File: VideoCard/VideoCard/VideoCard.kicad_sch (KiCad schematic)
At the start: 16 parts, among them J17 Conn_Coaxial, Q3 NPN, U12 TMS9918A, U16 74LS574, U17 74LS574, U18 74LS574, U19 HM62256BLP, U20 74HC04, U21 74LS138, Y1 Crystal

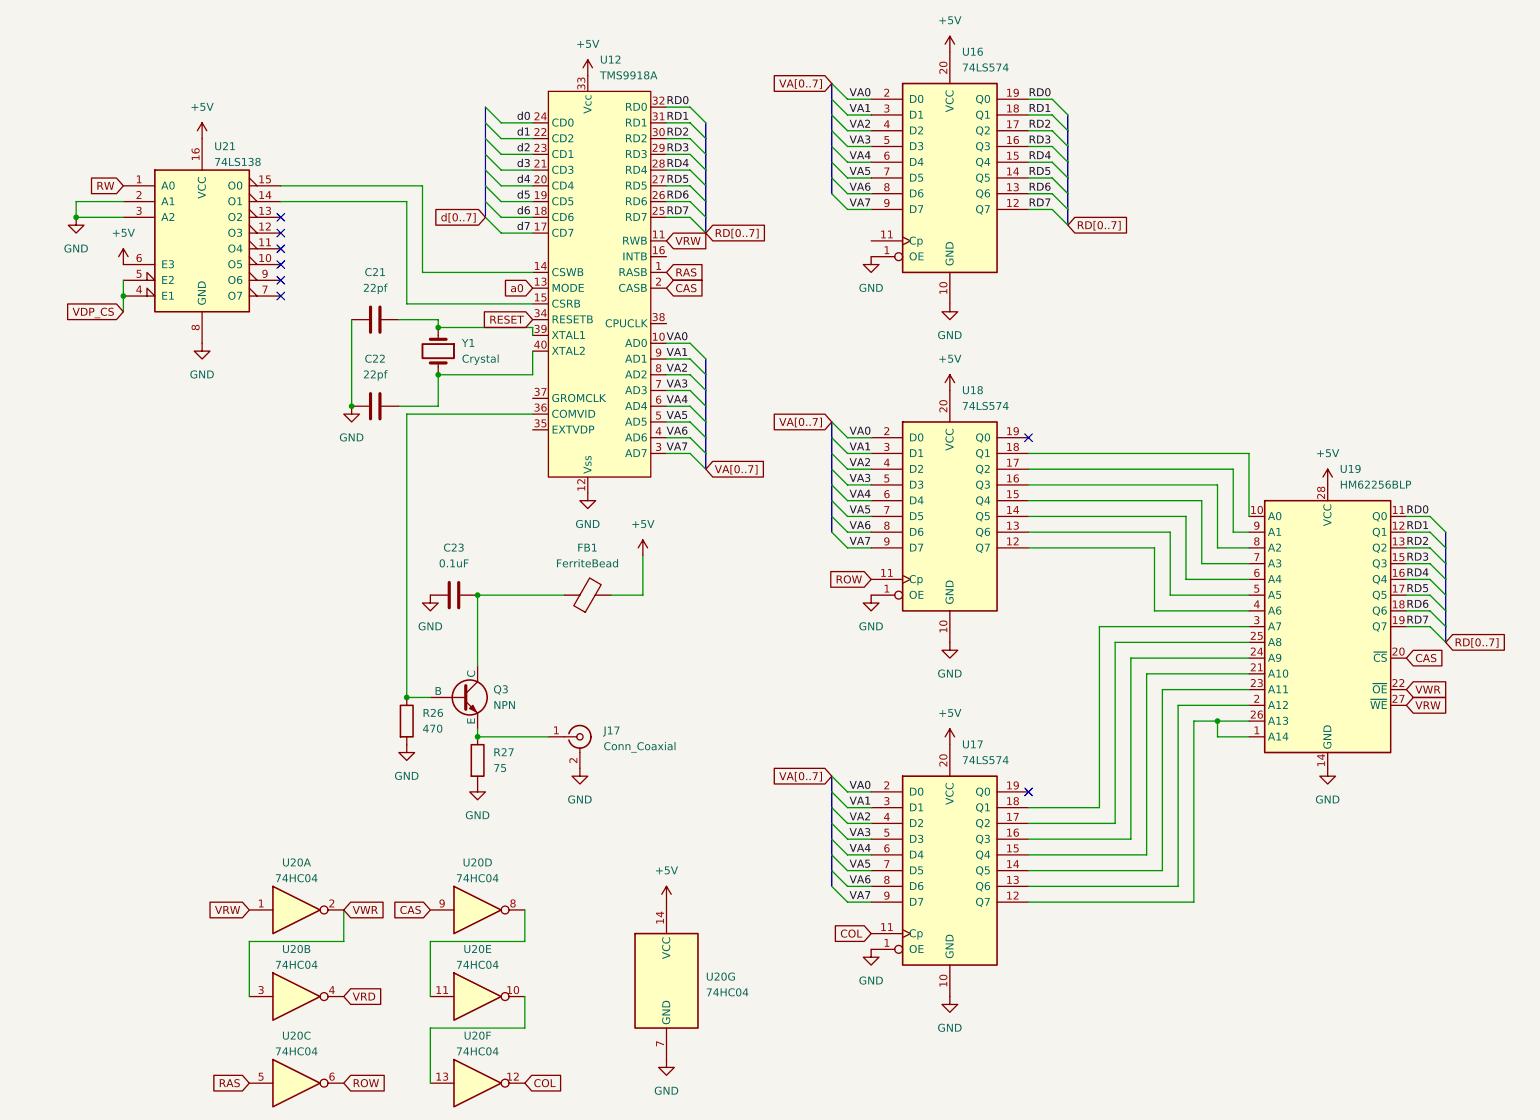
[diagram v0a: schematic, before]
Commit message: worked on new sound interface
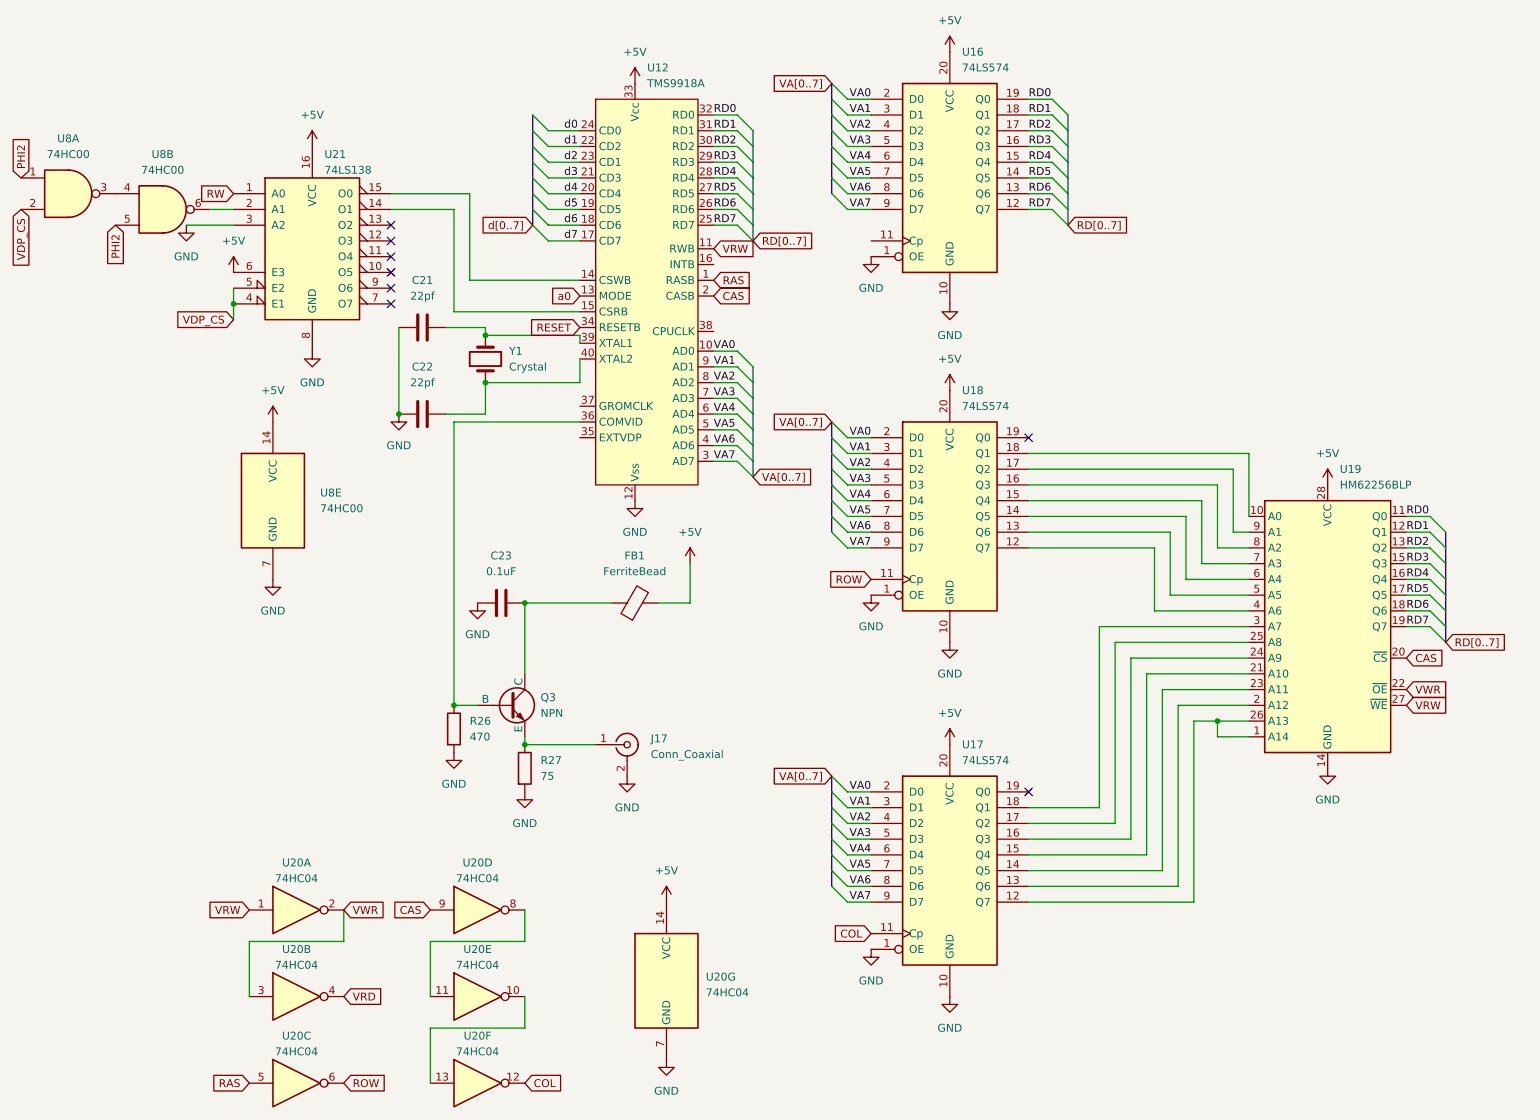
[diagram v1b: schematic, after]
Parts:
- added U8: 74HC00, symbol 74xx:74HC00
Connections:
- net +5V: now also U8.14 (VCC)
- net GND: now also U8.7 (GND); no longer U21.2 (A1)
- net VDP_CS: now also U8.2
- new net: U21.2 (A1), U8.6
- new net: U8.3, U8.4
- new net PHI2: U8.1, U8.5
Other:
- moved on the sheet: C21, C22, C23, FB1, J17, Q3, R26, R27, U12, U21, Y1

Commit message: changes
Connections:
- net PHI2: no longer U8.1
- net VDP_CS: now also U8.1
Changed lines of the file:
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@@
+    (stroke (width 0) (type default))
+  )
+  (wire (pts (xy 13.97 41.91) (xy 13.97 46.99))
     (stroke (width 0) (type default))
   )
@@
       (effects (font (size 1.27 1.27)) (justify left) hide)
     )
-  )
-  (global_label "PHI2" (shape input) (at 13.97 41.91 90) (fields_autoplaced)
-    (effects (font (size 1.27 1.27)) (justify left))
-    (property "Intersheetrefs" "${INTERSHEET_REFS}" (at 13.97 34.5894 90)
-      (effects (font (size 1.27 1.27)) (justify left) hide)
-    )
